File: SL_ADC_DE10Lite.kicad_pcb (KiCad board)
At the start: 4 copper layers, 98 x 67 mm, 33 parts, among them J1 DE10Lite header, J2 Analog header

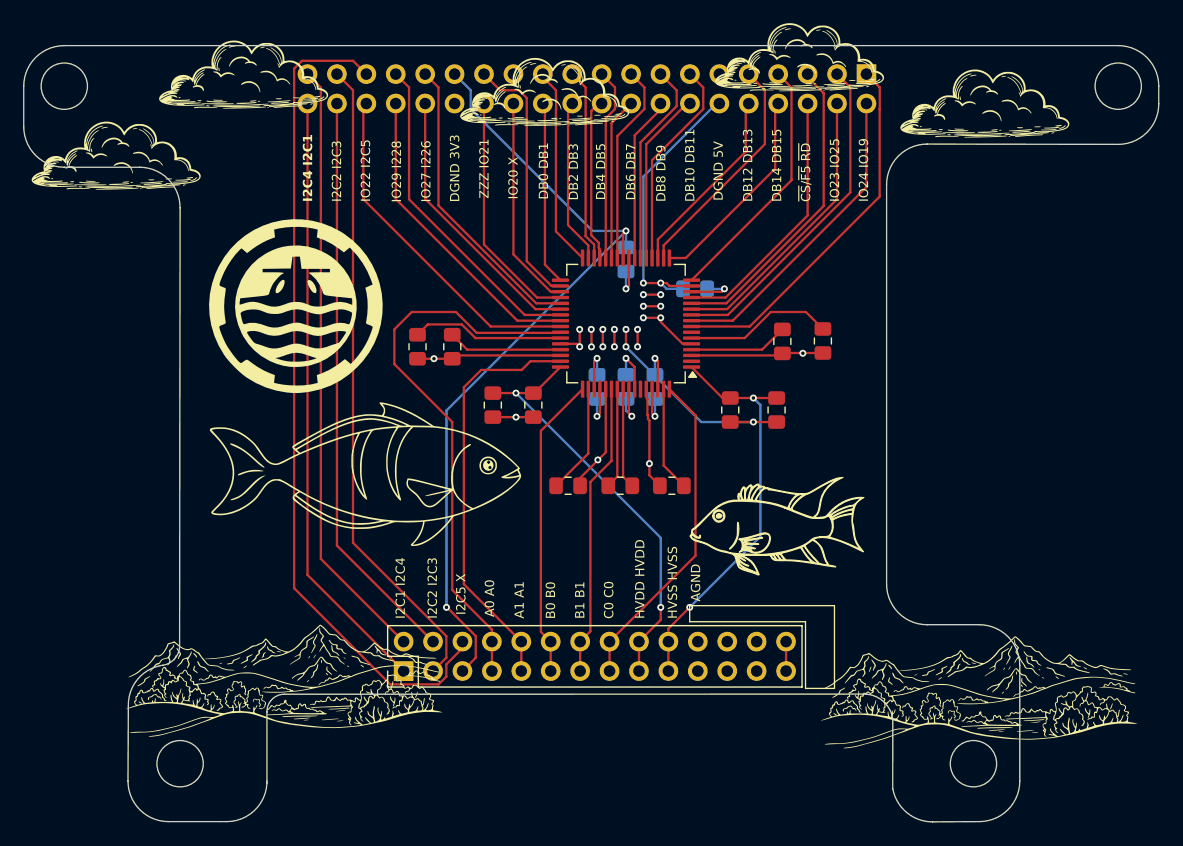
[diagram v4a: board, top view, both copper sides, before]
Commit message: Add power trace
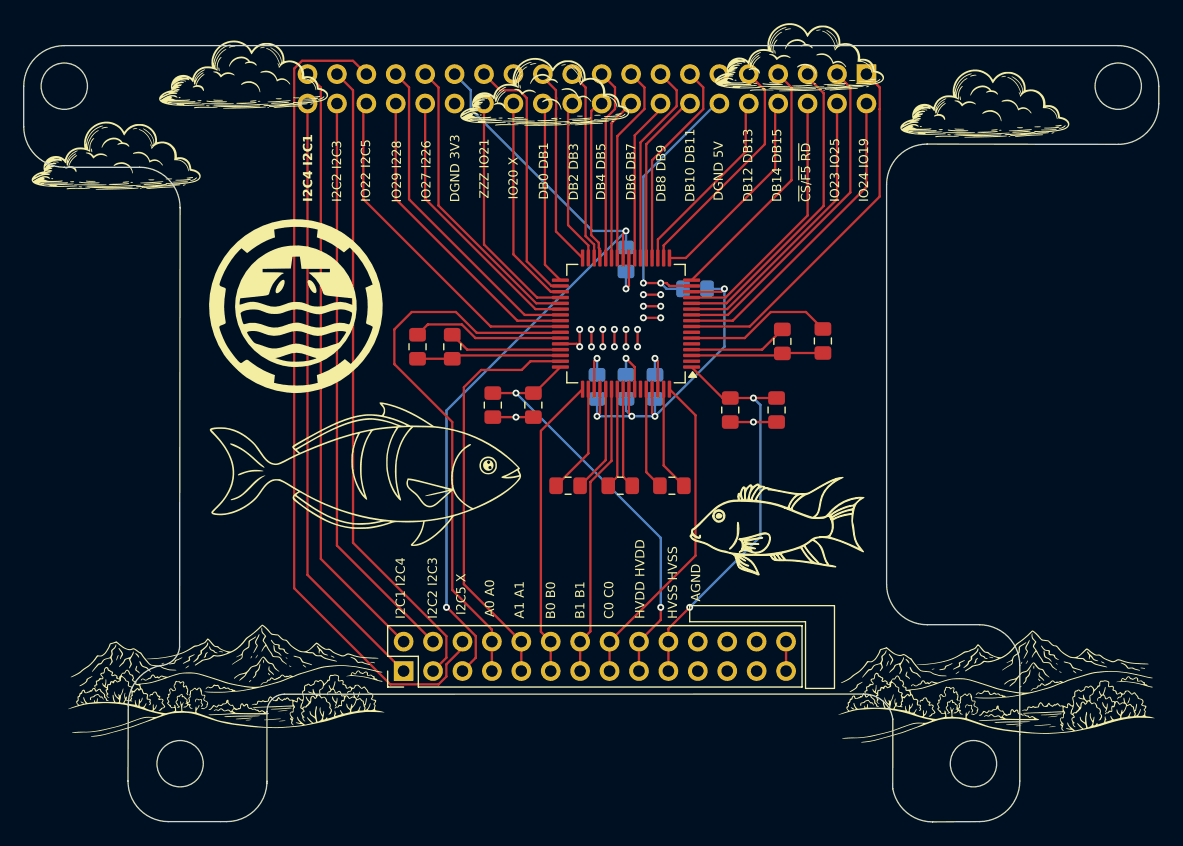
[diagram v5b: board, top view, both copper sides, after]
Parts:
- moved ? 5.00 mm to (77.5, 104.5)
- moved ? 1.58 mm to (144.0, 105.0)
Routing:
- net /AVDD: track 34.9 -> 53.4 mm
- net /AGND: track 126.4 -> 108.9 mm, vias 30 -> 26
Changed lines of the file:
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@@
 	(footprint "PCBDrawings:Mountains"
 		(layer "F.Cu")
-		(at 142.5 105.5)
+		(at 144 105)
 		(property "Reference" ""
 			(at 0 0 0)
@@
 	(footprint "PCBDrawings:Mountains"
 		(layer "F.Cu")
-		(at 82.5 104.5)
+		(at 77.5 104.5)
 		(property "Reference" ""
 			(at 0 0 0)
@@
 	(gr_line
 		(start 69 113.5)
-		(end 69.030968 107.005976)
+		(end 69.022543 107.000278)
 		(stroke
 			(width 0.1)
@@
 	)
 	(gr_arc
-		(start 69.030968 107.005976)
-		(mid 69.787179 104.761662)
-		(end 71.81 103.53)
+		(start 69.022543 107.000278)
+		(mid 69.778755 104.755964)
+		(end 71.801578 103.524302)
 		(stroke
 			(width 0.1)
@@
 	(gr_line
 		(start 72 103.5)
-		(end 71.81 103.53)
+		(end 71.803412 103.533458)
 		(stroke
 			(width 0.1)
@@
 	)
 	(segment
-		(start 114.02 82.368529)
-		(end 113.9 82.248529)
-		(width 0.2)
-		(layer "F.Cu")
-		(net "/AGND")
-	)
-	(segment
-		(start 113.9 81.965686)
-		(end 113.85 81.915685)
-		(width 0.2)
-		(layer "F.Cu")
-		(net "/AGND")
-	)
-	(segment
 		(start 109.017961 74.517961)
 		(end 109 74.5)
@@
 	)
 	(segment
-		(start 115 73.85741)
-		(end 115 73.5)
-		(width 0.2)
-		(layer "F.Cu")
-		(net "/AGND")
-	)
-	(segment
 		(start 112 77)
 		(end 112.75 77.75)
@@
 	)
 	(segment
-		(start 113.8 79.7125)
-		(end 113.75 79.6625)
-		(width 0.2)
-		(layer "F.Cu")
-		(net "/AGND")
-	)
-	(segment
 		(start 102.5 82.075)
 		(end 100.5 82.075)
@@
 	)
 	(segment
-		(start 108.0375 88)
-		(end 108.0375 87.3325)
+		(start 110.25 85.7875)
+		(end 110.25 79.6625)
 		(width 0.2)
 		(layer "F.Cu")
@@
 	)
 	(segment
-		(start 113.8 80.48241)
-		(end 113.8 79.7125)
-		(width 0.2)
-		(layer "F.Cu")
-		(net "/AGND")
-	)
-	(segment
-		(start 117.6625 75.75)
-		(end 116.89259 75.75)
+		(start 113.75 86.825)
+		(end 113.75 79.6625)
 		(width 0.2)
 		(layer "F.Cu")
@@
 	)
 	(segment
-		(start 114.02 87.095)
-		(end 114.02 82.368529)
+		(start 114.925 88)
+		(end 113.75 86.825)
 		(width 0.2)
 		(layer "F.Cu")
@@
 	)
 	(segment
-		(start 116.89259 75.75)
-		(end 115 73.85741)
-		(width 0.2)
-		(layer "F.Cu")
-		(net "/AGND")
-	)
-	(segment
-		(start 113.85 81.915685)
-		(end 113.85 80.53241)
-		(width 0.2)
-		(layer "F.Cu")
-		(net "/AGND")
-	)
-	(segment
-		(start 113.85 80.53241)
-		(end 113.8 80.48241)
-		(width 0.2)
-		(layer "F.Cu")
-		(net "/AGND")
-	)
-	(segment
 		(start 112.75 77.75)
 		(end 112.75 79.6625)
@@
 	)
 	(segment
-		(start 110.25 85.12)
-		(end 110.25 79.6625)
-		(width 0.2)
-		(layer "F.Cu")
-		(net "/AGND")
-	)
-	(segment
 		(start 113 76)
 		(end 113 74.5)
@@
 	)
 	(segment
-		(start 114.925 88)
-		(end 114.02 87.095)
-		(width 0.2)
-		(layer "F.Cu")
-		(net "/AGND")
-	)
-	(segment
 		(start 97.2875 76.75)
 		(end 106.3375 76.75)
@@
 	)
 	(segment
-		(start 108.0375 87.3325)
-		(end 110.25 85.12)
+		(start 108.0375 88)
+		(end 110.25 85.7875)
 		(width 0.2)
 		(layer "F.Cu")
@@
 		(net "/AGND")
 	)
-	(segment
-		(start 113.9 82.248529)
-		(end 113.9 81.965686)
-		(width 0.2)
-		(layer "F.Cu")
-		(net "/AGND")
-	)
-	(via
-		(at 127.27 76.56)
-		(size 0.6)
-		(drill 0.3)
-		(layers "F.Cu" "B.Cu")
-		(net "/AGND")
-	)
 	(via
 		(at 113 76)
@@
 	)
 	(via
-		(at 114.02 86.09)
-		(size 0.6)
-		(drill 0.3)
-		(layers "F.Cu" "B.Cu")
-		(net "/AGND")
-	)
-	(via
 		(at 109 74.5)
 		(size 0.6)
@@
 	)
 	(via
-		(at 95.42 77.03)
-		(size 0.6)
-		(drill 0.3)
-		(layers "F.Cu" "B.Cu")
-		(net "/AGND")
-	)
-	(via
 		(at 115 70.5)
 		(size 0.6)
@@
 	)
 	(via
-		(at 109.57 85.77)
-		(size 0.6)
-		(drill 0.3)
-		(layers "F.Cu" "B.Cu")
-		(net "/AGND")
-	)
-	(via
 		(at 108 76)
 		(size 0.6)
@@
 	)
 	(segment
-		(start 118.5 82.5)
-		(end 112 76)
-		(width 0.2)
-		(layer "B.Cu")
-		(net "/AGND")
-	)
-	(segment
 		(start 114.5 77)
 		(end 114.5 78.425)
@@
 	)
 	(segment
-		(start 123 82.5)
-		(end 118.5 82.5)
-		(width 0.2)
-		(layer "B.Cu")
-		(net "/AGND")
-	)
-	(segment
 		(start 113.5 61.3)
 		(end 119.8 55)
@@
 	)
 	(segment
+		(start 112.5 82)
+		(end 114.5 82)
+		(width 0.2)
+		(layer "B.Cu")
+		(net "/AVDD")
+	)
+	(segment
 		(start 114.5 80.5)
 		(end 114.5 82)
@@
 	)
 	(segment
+		(start 120.5 76)
+		(end 120.5 71)
+		(width 0.2)
+		(layer "B.Cu")
+		(net "/AVDD")
+	)
+	(segment
 		(start 112 81.5)
 		(end 112.5 82)
 		(width 0.2)
+		(layer "B.Cu")
+		(net "/AVDD")
+	)
+	(segment
+		(start 114.5 82)
+		(end 120.5 76)
+		(width 0.2)
+		(layer "B.Cu")
+		(net "/AVDD")
+	)
+	(segment
+		(start 109.5 82)
+		(end 112.5 82)
+		(width 0.2)

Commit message: fixed some missing connections, more to go
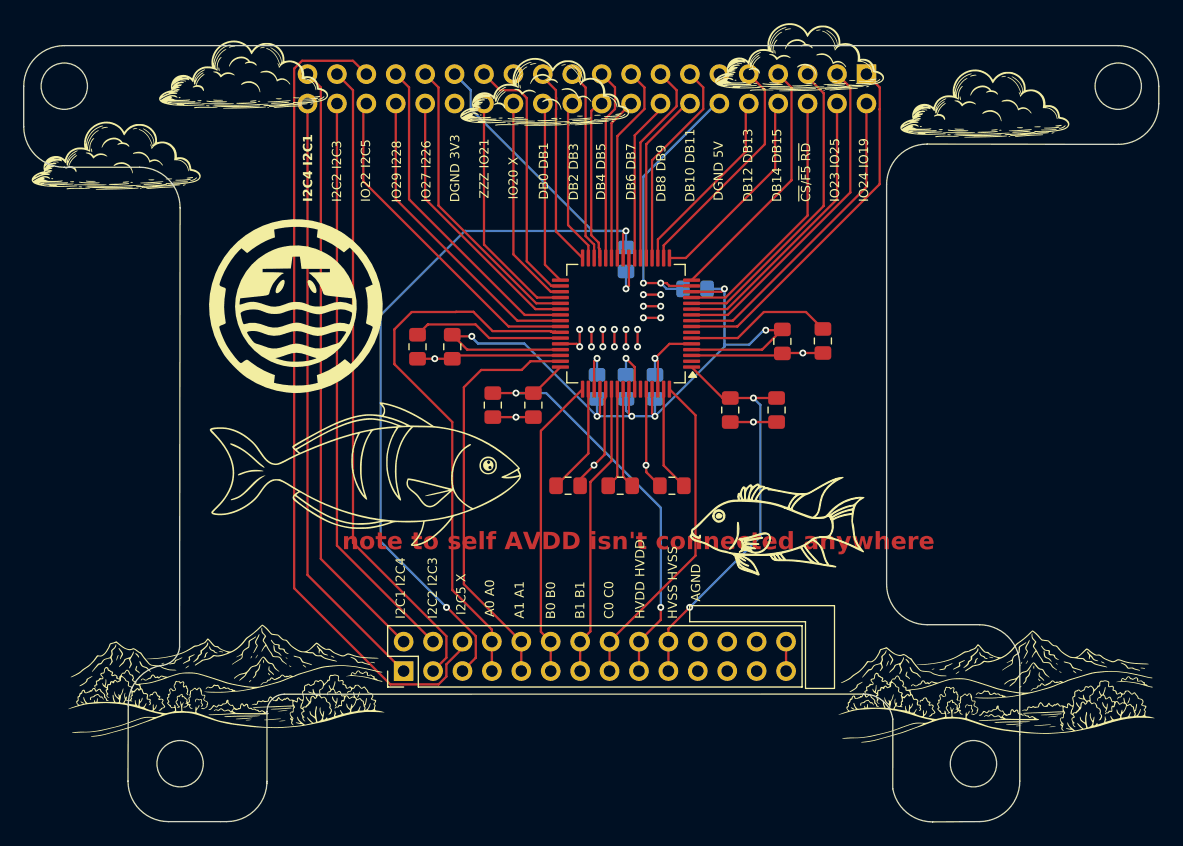
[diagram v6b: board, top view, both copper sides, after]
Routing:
- net /AVDD: track 53.4 -> 74.4 mm, vias 4 -> 6
- net /DVDD: track 71.2 -> 84.1 mm
- net /AGND: track 108.9 -> 112.6 mm, vias 26 -> 30
- net /HVDD: track 36.7 -> 38.3 mm
- net /GPIO(22)-~{HW}/SW: track 29.9 -> 29.0 mm
- net /GPIO(19)-~{PAR}/SER: track 31.9 -> 31.3 mm
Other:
- board text added: "note to self AVDD isn't connected anywhere"
